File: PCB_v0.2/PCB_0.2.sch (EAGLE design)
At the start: 35 parts, among them IC1 MEGA8_-AU, T1 BC847, T2 BC847, T3 BC847, T4 BC847

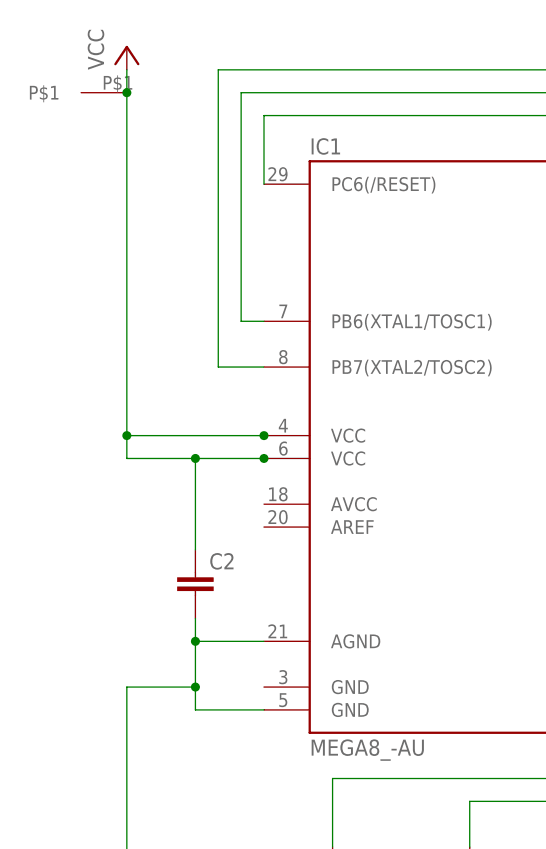
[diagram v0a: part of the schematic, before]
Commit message: Complete reup
- couple of minor bugs fixed
- PCB update
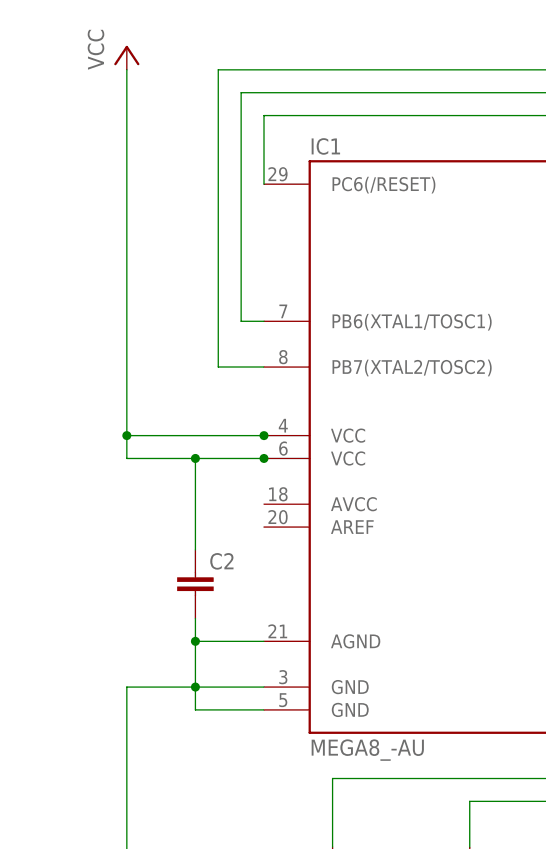
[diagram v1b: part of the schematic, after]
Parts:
- removed PC6: Fahrkanal, Pad:PAD
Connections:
- net GND: now also IC1.GND@1
- net VCC: no longer PC6.P$1
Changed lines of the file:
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@@
 <part name="PC4" library="Pad" deviceset="PAD" device="" value="Fahrkanal"/>
 <part name="PC5" library="Pad" deviceset="PAD" device="" value="Fahrkanal"/>
-<part name="PC6" library="Pad" deviceset="PAD" device="" value="Fahrkanal"/>
 <part name="U$1" library="Pad" deviceset="PAD" device=""/>
 <part name="C2" library="resistor" deviceset="C-EU" device="C0603K"/>
@@
 <instance part="PC4" gate="G$1" x="66.04" y="-86.36"/>
 <instance part="PC5" gate="G$1" x="-45.72" y="-93.98" rot="R180"/>
-<instance part="PC6" gate="G$1" x="-45.72" y="22.86" rot="R180"/>
 <instance part="U$1" gate="G$1" x="66.04" y="-22.86"/>
 <instance part="C2" gate="G$1" x="-38.1" y="-30.48"/>
@@
 <pinref part="C2" gate="G$1" pin="2"/>
 <wire x1="-38.1" y1="-35.56" x2="-38.1" y2="-38.1" width="0.1524" layer="91"/>
-<pinref part="IC1" gate="1" pin="AGND"/>
+<pinref part="IC1" gate="1" pin="GND@2"/>
 <wire x1="-38.1" y1="-38.1" x2="-38.1" y2="-43.18" width="0.1524" layer="91"/>
-<wire x1="-30.48" y1="-38.1" x2="-38.1" y2="-38.1" width="0.1524" layer="91"/>
-<junction x="-38.1" y="-38.1"/>
-<pinref part="IC1" gate="1" pin="GND@2"/>
 <wire x1="-30.48" y1="-45.72" x2="-38.1" y2="-45.72" width="0.1524" layer="91"/>
 <wire x1="-38.1" y1="-45.72" x2="-38.1" y2="-43.18" width="0.1524" layer="91"/>
 <junction x="-38.1" y="-43.18"/>
+<pinref part="IC1" gate="1" pin="GND@1"/>
+<wire x1="-38.1" y1="-43.18" x2="-30.48" y2="-43.18" width="0.1524" layer="91"/>
+<pinref part="IC1" gate="1" pin="AGND"/>
+<wire x1="-30.48" y1="-38.1" x2="-38.1" y2="-38.1" width="0.1524" layer="91"/>
+<junction x="-38.1" y="-38.1"/>
 </segment>
 </net>
@@
 <wire x1="30.48" y1="-33.02" x2="66.04" y2="-33.02" width="0.1524" layer="91"/>
 <pinref part="U$16" gate="G$1" pin="P$1"/>
-</segment>
-</net>
-<net name="VCC" class="0">
-<segment>
-<pinref part="P+1" gate="VCC" pin="VCC"/>
-<wire x1="-45.72" y1="25.4" x2="-45.72" y2="22.86" width="0.1524" layer="91"/>
-<pinref part="PC6" gate="G$1" pin="P$1"/>
-<pinref part="IC1" gate="1" pin="VCC@2"/>
-<wire x1="-30.48" y1="-17.78" x2="-38.1" y2="-17.78" width="0.1524" layer="91"/>
-<wire x1="-38.1" y1="-17.78" x2="-45.72" y2="-17.78" width="0.1524" layer="91"/>
-<wire x1="-45.72" y1="-17.78" x2="-45.72" y2="-15.24" width="0.1524" layer="91"/>
-<junction x="-45.72" y="22.86"/>
-<pinref part="IC1" gate="1" pin="VCC@1"/>
-<wire x1="-45.72" y1="-15.24" x2="-45.72" y2="22.86" width="0.1524" layer="91"/>
-<wire x1="-30.48" y1="-15.24" x2="-45.72" y2="-15.24" width="0.1524" layer="91"/>
-<junction x="-45.72" y="-15.24"/>
-<junction x="-30.48" y="-15.24"/>
-<junction x="-30.48" y="-17.78"/>
-<pinref part="C2" gate="G$1" pin="1"/>
-<wire x1="-38.1" y1="-27.94" x2="-38.1" y2="-17.78" width="0.1524" layer="91"/>
-<junction x="-38.1" y="-17.78"/>
 </segment>
 </net>
@@
 </segment>
 </net>
+<net name="VCC" class="0">
+<segment>
+<pinref part="IC1" gate="1" pin="VCC@2"/>
+<wire x1="-30.48" y1="-17.78" x2="-38.1" y2="-17.78" width="0.1524" layer="91"/>
+<wire x1="-38.1" y1="-17.78" x2="-45.72" y2="-17.78" width="0.1524" layer="91"/>
+<wire x1="-45.72" y1="-17.78" x2="-45.72" y2="-15.24" width="0.1524" layer="91"/>
+<pinref part="IC1" gate="1" pin="VCC@1"/>
+<wire x1="-30.48" y1="-15.24" x2="-45.72" y2="-15.24" width="0.1524" layer="91"/>
+<junction x="-30.48" y="-15.24"/>
+<junction x="-30.48" y="-17.78"/>
+<pinref part="C2" gate="G$1" pin="1"/>
+<wire x1="-38.1" y1="-27.94" x2="-38.1" y2="-17.78" width="0.1524" layer="91"/>
+<junction x="-38.1" y="-17.78"/>
+<pinref part="P+1" gate="VCC" pin="VCC"/>
+<wire x1="-45.72" y1="25.4" x2="-45.72" y2="-15.24" width="0.1524" layer="91"/>
+<junction x="-45.72" y="-15.24"/>
+</segment>
+</net>
